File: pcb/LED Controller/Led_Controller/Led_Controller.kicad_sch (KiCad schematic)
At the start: 22 parts

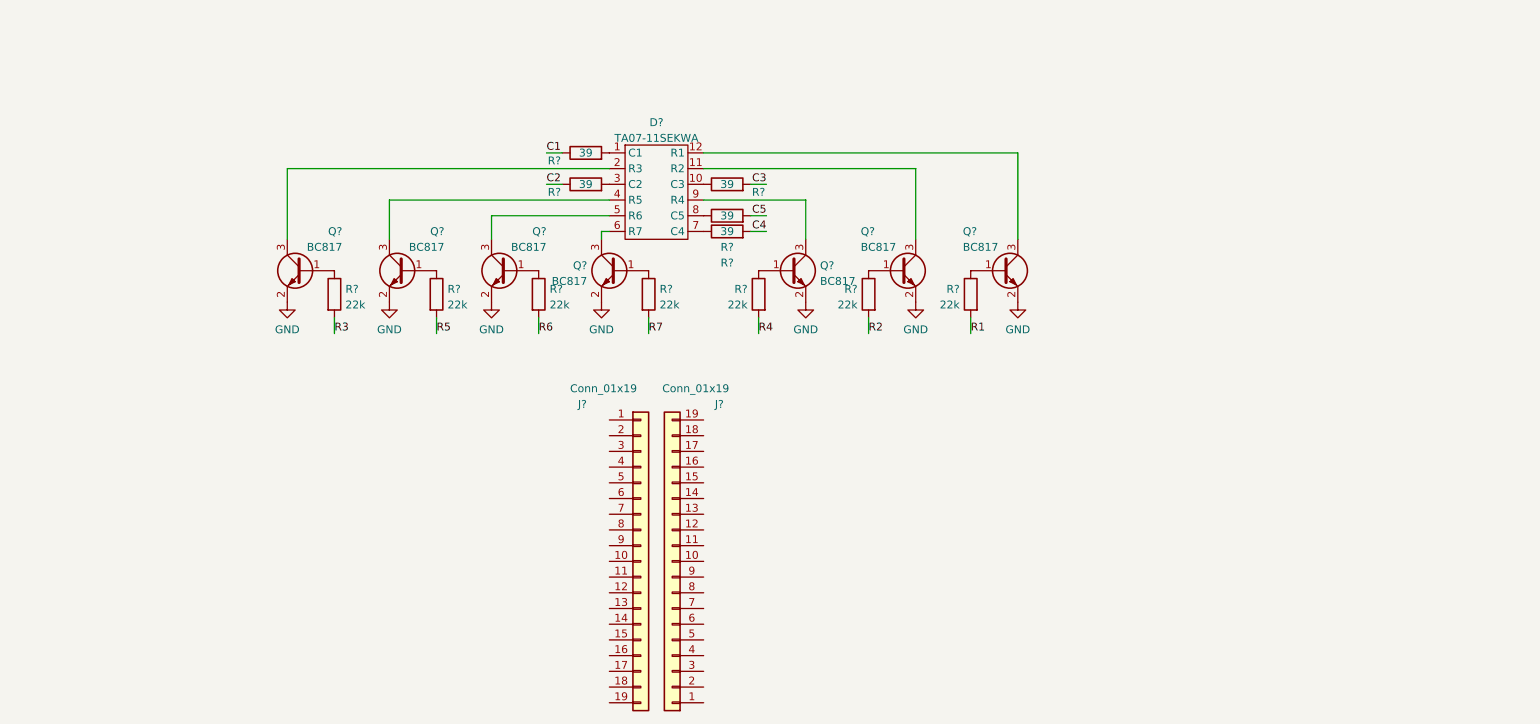
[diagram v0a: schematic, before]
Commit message: edit docs 9 add puml
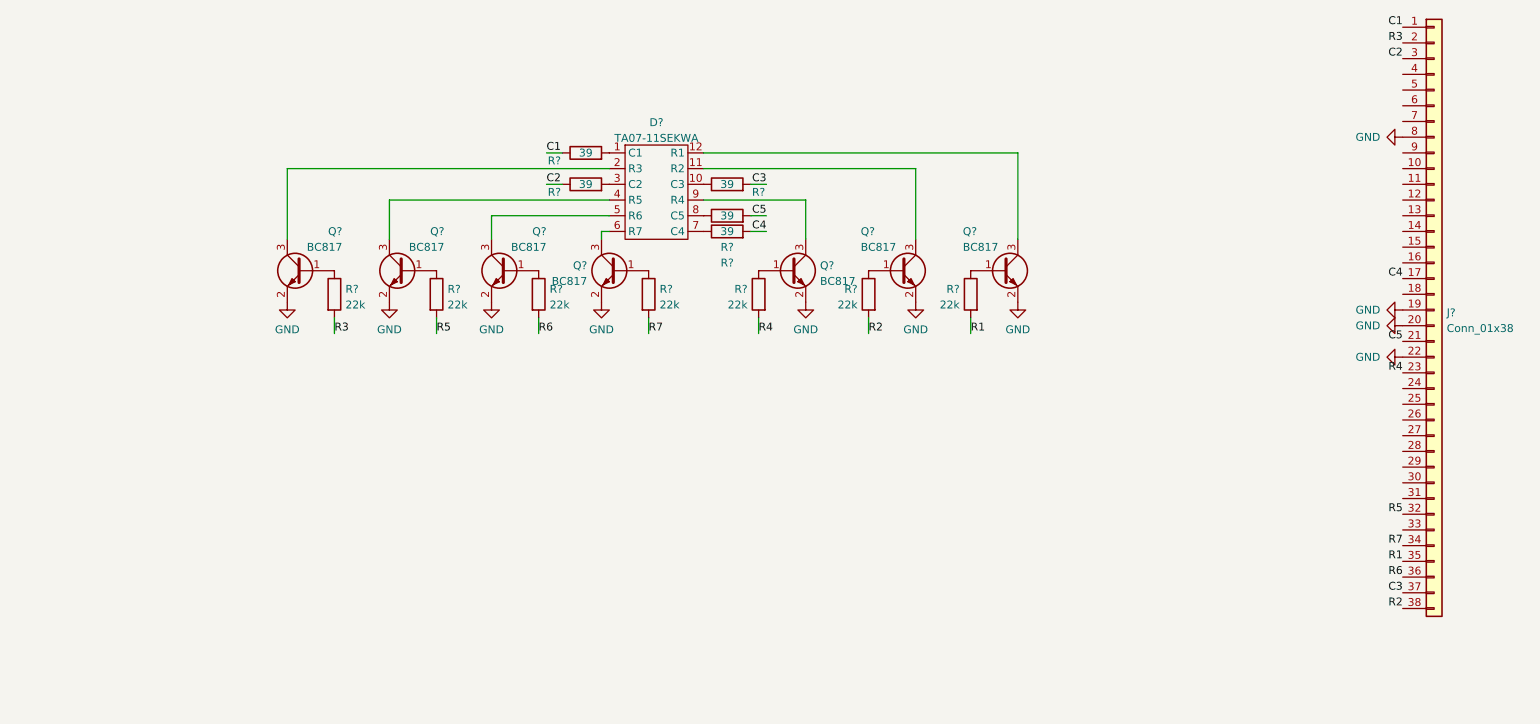
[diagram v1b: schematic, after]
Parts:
- removed J? (x2): Conn_01x19, symbol Connector_Generic:Conn_01x19
- added J?: Conn_01x38, symbol Connector_Generic:Conn_01x38
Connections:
- net C1: now also J?.1 (Pin_1)
- net C2: now also J?.3 (Pin_3)
- net C3: now also J?.37 (Pin_37)
- net C4: now also J?.17 (Pin_17)
- net C5: now also J?.21 (Pin_21)
- net GND: now also J?.19 (Pin_19), J?.20 (Pin_20), J?.22 (Pin_22), J?.8 (Pin_8)
- net R1: now also J?.35 (Pin_35)
- net R2: now also J?.38 (Pin_38)
- net R3: now also J?.2 (Pin_2)
- net R4: now also J?.23 (Pin_23)
- net R5: now also J?.32 (Pin_32)
- net R6: now also J?.36 (Pin_36)
- net R7: now also J?.34 (Pin_34)
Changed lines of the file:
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@@
     (effects (font (size 1.27 1.27)) (justify left bottom))
+  )
+  (label "R7" (at 252.73 115.57 180)
+    (effects (font (size 1.27 1.27)) (justify right bottom))
+  )
+  (label "C5" (at 252.73 82.55 180)
+    (effects (font (size 1.27 1.27)) (justify right bottom))
   )
   (label "R3" (at 80.01 81.28 0)
@@
     (effects (font (size 1.27 1.27)) (justify right bottom))
   )
+  (label "R6" (at 252.73 120.65 180)
+    (effects (font (size 1.27 1.27)) (justify right bottom))
+  )
   (label "C2" (at 114.3 57.15 0)
     (effects (font (size 1.27 1.27)) (justify left bottom))
   )
+  (label "R3" (at 252.73 34.29 180)
+    (effects (font (size 1.27 1.27)) (justify right bottom))
+  )
+  (label "R5" (at 252.73 110.49 180)
+    (effects (font (size 1.27 1.27)) (justify right bottom))
+  )
+  (label "R1" (at 252.73 118.11 180)
+    (effects (font (size 1.27 1.27)) (justify right bottom))
+  )
   (label "R2" (at 166.37 81.28 0)
     (effects (font (size 1.27 1.27)) (justify left bottom))
@@
     (effects (font (size 1.27 1.27)) (justify right bottom))
   )
+  (label "R4" (at 252.73 87.63 180)
+    (effects (font (size 1.27 1.27)) (justify right bottom))
+  )
   (label "C4" (at 149.86 64.77 180)
     (effects (font (size 1.27 1.27)) (justify right bottom))
   )
+  (label "C2" (at 252.73 36.83 180)
+    (effects (font (size 1.27 1.27)) (justify right bottom))
+  )
+  (label "C1" (at 252.73 31.75 180)
+    (effects (font (size 1.27 1.27)) (justify right bottom))
+  )
   (label "R7" (at 130.81 81.28 0)
     (effects (font (size 1.27 1.27)) (justify left bottom))
+  )
+  (label "C3" (at 252.73 123.19 180)
+    (effects (font (size 1.27 1.27)) (justify right bottom))
+  )
+  (label "R2" (at 252.73 125.73 180)
+    (effects (font (size 1.27 1.27)) (justify right bottom))
+  )
+  (label "C4" (at 252.73 72.39 180)
+    (effects (font (size 1.27 1.27)) (justify right bottom))
   )
   (label "R4" (at 148.59 81.28 0)
@@
     (pin "3")
   )
+  (symbol (lib_id "power:GND") (at 252.73 80.01 270) (mirror x) (unit 1)
+    (in_bom yes) (on_board yes)
+    (property "Reference" "#PWR?" (id 0) (at 246.38 80.01 0)
+      (effects (font (size 1.27 1.27)) hide)
+    )
+    (property "Value" "GND" (id 1) (at 245.11 80.01 90)
+      (effects (font (size 1.27 1.27)) (justify left))
+    )
+    (property "Footprint" "" (id 2) (at 252.73 80.01 0)
+      (effects (font (size 1.27 1.27)) hide)
+    )
+    (property "Datasheet" "" (id 3) (at 252.73 80.01 0)
+      (effects (font (size 1.27 1.27)) hide)
+    )
+    (pin "1")
+  )
   (symbol (lib_id "power:GND") (at 88.9 76.2 0) (unit 1)
     (in_bom yes) (on_board yes) (fields_autoplaced)
@@
     (pin "1")
     (pin "2")
+  )
+  (symbol (lib_id "power:GND") (at 252.73 49.53 270) (mirror x) (unit 1)
+    (in_bom yes) (on_board yes)
+    (property "Reference" "#PWR?" (id 0) (at 246.38 49.53 0)
+      (effects (font (size 1.27 1.27)) hide)
+    )
+    (property "Value" "GND" (id 1) (at 245.11 49.53 90)
+      (effects (font (size 1.27 1.27)) (justify left))
+    )
+    (property "Footprint" "" (id 2) (at 252.73 49.53 0)
+      (effects (font (size 1.27 1.27)) hide)
+    )
+    (property "Datasheet" "" (id 3) (at 252.73 49.53 0)
+      (effects (font (size 1.27 1.27)) hide)
+    )
+    (pin "1")
   )
   (symbol (lib_id "led_matrx TA07-11SEKWA:TA07-11SEKWA") (at 127 66.04 0) (unit 1)
@@
     (pin "1")
   )
-  (symbol (lib_id "Connector_Generic:Conn_01x19") (at 134.62 118.11 180) (unit 1)
-    (in_bom yes) (on_board yes)
-    (property "Reference" "J?" (id 0) (at 142.24 92.71 0))
-    (property "Value" "Conn_01x19" (id 1) (at 138.43 90.17 0))
-    (property "Footprint" "" (id 2) (at 134.62 118.11 0)
-      (effects (font (size 1.27 1.27)) hide)
-    )
-    (property "Datasheet" "~" (id 3) (at 134.62 118.11 0)
+  (symbol (lib_id "power:GND") (at 252.73 85.09 270) (mirror x) (unit 1)
+    (in_bom yes) (on_board yes)
+    (property "Reference" "#PWR?" (id 0) (at 246.38 85.09 0)
+      (effects (font (size 1.27 1.27)) hide)
+    )
+    (property "Value" "GND" (id 1) (at 245.11 85.09 90)
+      (effects (font (size 1.27 1.27)) (justify left))
+    )
+    (property "Footprint" "" (id 2) (at 252.73 85.09 0)
+      (effects (font (size 1.27 1.27)) hide)
+    )
+    (property "Datasheet" "" (id 3) (at 252.73 85.09 0)
+      (effects (font (size 1.27 1.27)) hide)
+    )
+    (pin "1")
+  )
+  (symbol (lib_id "power:GND") (at 252.73 77.47 270) (mirror x) (unit 1)
+    (in_bom yes) (on_board yes)
+    (property "Reference" "#PWR?" (id 0) (at 246.38 77.47 0)
+      (effects (font (size 1.27 1.27)) hide)
+    )
+    (property "Value" "GND" (id 1) (at 245.11 77.47 90)
+      (effects (font (size 1.27 1.27)) (justify left))
+    )
+    (property "Footprint" "" (id 2) (at 252.73 77.47 0)
+      (effects (font (size 1.27 1.27)) hide)
+    )
+    (property "Datasheet" "" (id 3) (at 252.73 77.47 0)
+      (effects (font (size 1.27 1.27)) hide)
+    )
+    (pin "1")
+  )
+  (symbol (lib_id "Transistor_BJT:BC817") (at 187.96 71.12 0) (unit 1)
+    (in_bom yes) (on_board yes)
+    (property "Reference" "Q?" (id 0) (at 181.61 64.77 0)
+      (effects (font (size 1.27 1.27)) (justify left))
+    )
+    (property "Value" "BC817" (id 1) (at 181.61 67.3069 0)
+      (effects (font (size 1.27 1.27)) (justify left))
+    )
+    (property "Footprint" "Package_TO_SOT_SMD:SOT-23" (id 2) (at 193.04 73.025 0)
+      (effects (font (size 1.27 1.27) italic) (justify left) hide)
+    )
+    (property "Datasheet" "https://www.onsemi.com/pub/Collateral/BC818-D.pdf" (id 3) (at 187.96 71.12 0)
+      (effects (font (size 1.27 1.27)) (justify left) hide)
+    )
+    (pin "1")
+    (pin "2")
+    (pin "3")
+  )
+  (symbol (lib_id "Connector_Generic:Conn_01x38") (at 257.81 77.47 0) (unit 1)
+    (in_bom yes) (on_board yes) (fields_autoplaced)
+    (property "Reference" "J?" (id 0) (at 259.842 77.9053 0)
+      (effects (font (size 1.27 1.27)) (justify left))
+    )
+    (property "Value" "Conn_01x38" (id 1) (at 259.842 80.4422 0)
+      (effects (font (size 1.27 1.27)) (justify left))
+    )
+    (property "Footprint" "" (id 2) (at 257.81 77.47 0)
+      (effects (font (size 1.27 1.27)) hide)
+    )
+    (property "Datasheet" "~" (id 3) (at 257.81 77.47 0)
       (effects (font (size 1.27 1.27)) hide)
     )
@@
     (pin "19")
     (pin "2")
-    (pin "3")
+    (pin "20")
+    (pin "21")
+    (pin "22")
+    (pin "23")
+    (pin "24")
+    (pin "25")
+    (pin "26")
+    (pin "27")
+    (pin "28")
+    (pin "29")
+    (pin "3")
+    (pin "30")
+    (pin "31")
+    (pin "32")
+    (pin "33")
+    (pin "34")
+    (pin "35")
+    (pin "36")
+    (pin "37")
+    (pin "38")
     (pin "4")
     (pin "5")
@@
     (pin "9")
   )
-  (symbol (lib_id "Connector_Generic:Conn_01x19") (at 129.54 118.11 0) (unit 1)
-    (in_bom yes) (on_board yes)
-    (property "Reference" "J?" (id 0) (at 119.38 92.71 0)
-      (effects (font (size 1.27 1.27)) (justify left))
-    )
-    (property "Value" "Conn_01x19" (id 1) (at 118.11 90.17 0)
-      (effects (font (size 1.27 1.27)) (justify left))
-    )
-    (property "Footprint" "" (id 2) (at 129.54 118.11 0)
-      (effects (font (size 1.27 1.27)) hide)
-    )
-    (property "Datasheet" "~" (id 3) (at 129.54 118.11 0)
-      (effects (font (size 1.27 1.27)) hide)
-    )
-    (pin "1")
-    (pin "10")
-    (pin "11")
-    (pin "12")
-    (pin "13")
-    (pin "14")
-    (pin "15")
-    (pin "16")
-    (pin "17")
-    (pin "18")
-    (pin "19")
-    (pin "2")
-    (pin "3")
-    (pin "4")
-    (pin "5")
-    (pin "6")
-    (pin "7")
-    (pin "8")
-    (pin "9")
-  )
-  (symbol (lib_id "Transistor_BJT:BC817") (at 187.96 71.12 0) (unit 1)
-    (in_bom yes) (on_board yes)
-    (property "Reference" "Q?" (id 0) (at 181.61 64.77 0)
-      (effects (font (size 1.27 1.27)) (justify left))
-    )
-    (property "Value" "BC817" (id 1) (at 181.61 67.3069 0)
-      (effects (font (size 1.27 1.27)) (justify left))
-    )
-    (property "Footprint" "Package_TO_SOT_SMD:SOT-23" (id 2) (at 193.04 73.025 0)
-      (effects (font (size 1.27 1.27) italic) (justify left) hide)
-    )
-    (property "Datasheet" "https://www.onsemi.com/pub/Collateral/BC818-D.pdf" (id 3) (at 187.96 71.12 0)
-      (effects (font (size 1.27 1.27)) (justify left) hide)
-    )
-    (pin "1")
-    (pin "2")
-    (pin "3")
-  )
   (symbol (lib_id "power:GND") (at 190.5 76.2 0) (mirror y) (unit 1)
     (in_bom yes) (on_board yes) (fields_autoplaced)
@@
       (reference "#PWR?") (unit 1) (value "GND") (footprint "")
     )
+    (path "/28db63c5-3e0f-4c65-a865-117d67c88267"
+      (reference "#PWR?") (unit 1) (value "GND") (footprint "")
+    )
     (path "/39b04c6a-a164-49f1-abea-a3a32285d465"
       (reference "#PWR?") (unit 1) (value "GND") (footprint "")
@@
       (reference "#PWR?") (unit 1) (value "GND") (footprint "")
     )
+    (path "/70815813-8fc8-447e-a7bf-e7cd5af3ba62"
+      (reference "#PWR?") (unit 1) (value "GND") (footprint "")
+    )
     (path "/8a2b69bf-21b6-4f4b-aef2-35e199d0dd46"
+      (reference "#PWR?") (unit 1) (value "GND") (footprint "")
+    )
+    (path "/a04d49d2-07a6-45c0-b682-9328e6046e78"
+      (reference "#PWR?") (unit 1) (value "GND") (footprint "")
+    )
+    (path "/b7729194-7e46-4c86-8f37-0ea3df1cad63"
       (reference "#PWR?") (unit 1) (value "GND") (footprint "")
     )
@@
       (reference "D?") (unit 1) (value "TA07-11SEKWA") (footprint "")
     )
-    (path "/912611b2-378a-460d-8970-50f247ed94ec"
-      (reference "J?") (unit 1) (value "Conn_01x19") (footprint "")
-    )
-    (path "/99fb0de9-22ac-4df6-a4b1-3b9893d762dc"
-      (reference "J?") (unit 1) (value "Conn_01x19") (footprint "")
+    (path "/d618548f-a200-4619-96bb-6d3c613c7ef6"
+      (reference "J?") (unit 1) (value "Conn_01x38") (footprint "")
     )
     (path "/24211bb3-d772-4c10-aec1-ecd36218d80c"

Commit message: add zip led Controller
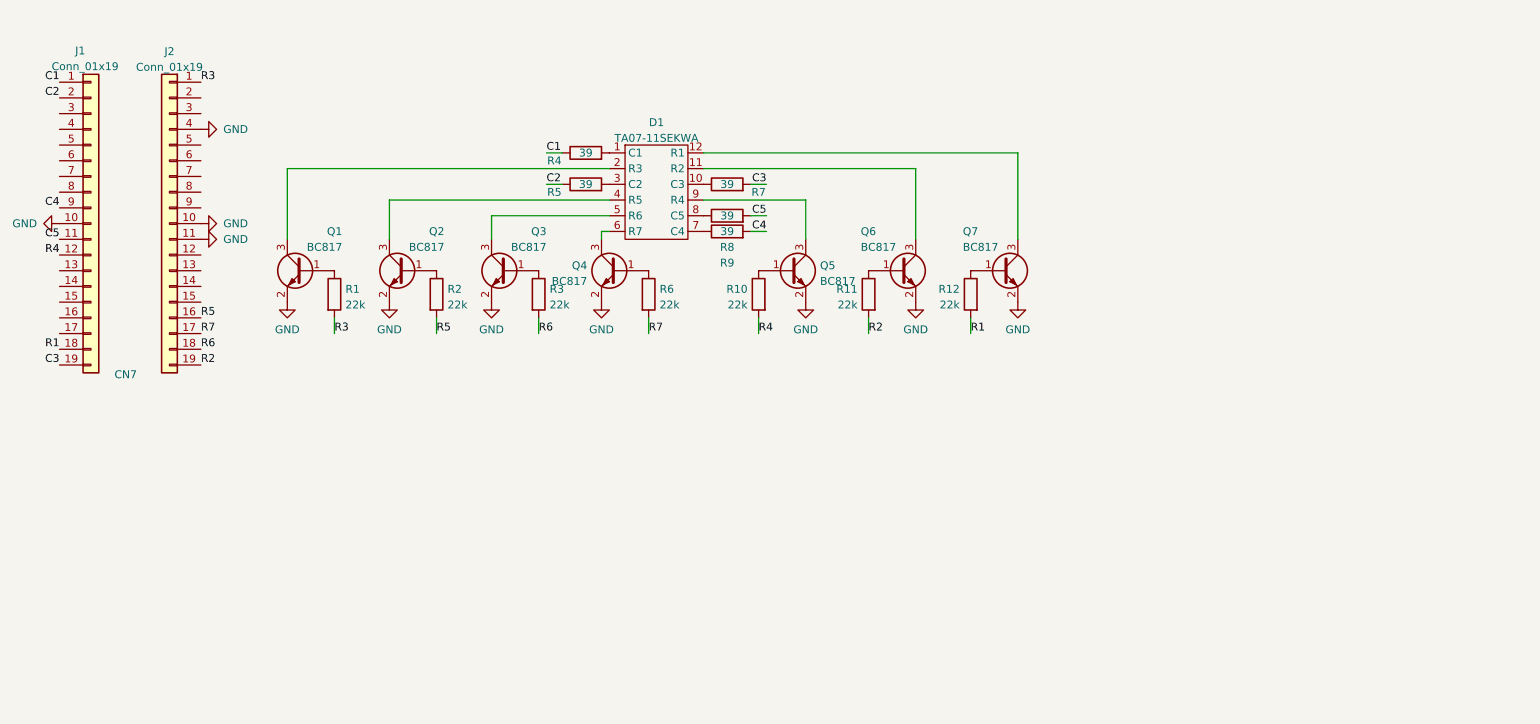
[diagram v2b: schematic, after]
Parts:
- removed J?: Conn_01x38, symbol Connector_Generic:Conn_01x38
- added J1, J2: Conn_01x19, symbol Connector_Generic:Conn_01x19
- gave numbers to parts that had none: 20
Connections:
- net C1: now also J1.1 (Pin_1)
- net C2: now also J1.2 (Pin_2)
- net C3: now also J1.19 (Pin_19)
- net C4: now also J1.9 (Pin_9)
- net C5: now also J1.11 (Pin_11)
- net GND: now also J1.10 (Pin_10), J2.10 (Pin_10), J2.11 (Pin_11), J2.4 (Pin_4)
- net R1: now also J1.18 (Pin_18)
- net R2: now also J2.19 (Pin_19)
- net R3: now also J2.1 (Pin_1)
- net R4: now also J1.12 (Pin_12)
- net R5: now also J2.16 (Pin_16)
- net R6: now also J2.18 (Pin_18)
- net R7: now also J2.17 (Pin_17)
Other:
- note added: "CN7"
